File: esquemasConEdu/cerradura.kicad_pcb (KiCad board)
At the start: 2 copper layers, 85.8 x 137 mm, 16 parts, among them Q1 PN2222A

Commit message: conectado
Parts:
- moved A3144 119.0 mm to (72.1, 176.9), turned to 180 degrees
- moved 10K1 117.8 mm to (61.0, 154.9), turned to -90 degrees
- moved MOTOR_BORN1 96.7 mm to (122.8, 176.7), turned to 180 degrees
- moved Q1 95.6 mm to (63.1, 150.7)
- moved BUZZER1 80.0 mm to (67.8, 139.7), turned to 180 degrees
- moved 5V_BORN1 76.8 mm to (123.2, 58.4), turned to -90 degrees
- moved RC522 50.3 mm to (93.4, 127.9), turned to 90 degrees
- moved lm2596hvs1 47.4 mm to (90.9, 60.3), turned to 0 degrees
- moved R305 38.9 mm to (58.4, 89.2)
- moved 12V-BORN1 30.9 mm to (54.5, 51.8), turned to 90 degrees
- moved SSD1306 26.0 mm to (107.9, 89.3), turned to 90 degrees
- moved DRV8825 25.7 mm to (95.5, 178.5)
- moved Keypad1 18.8 mm to (109.2, 160.7), turned to 180 degrees
- moved ESP1 10.5 mm to (113.6, 134.3)
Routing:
- net GND: track 0.00 -> 480.5 mm
- net +5V: track 0.00 -> 226.1 mm
- net +12V: track 0.00 -> 207.4 mm
- net +3.3V: track 0.00 -> 205.6 mm
- net /drv882x_en: track 0.00 -> 87.8 mm
- net /r305_rx: track 0.00 -> 78.4 mm
- net /ssd1306_scl: track 0.00 -> 77.1 mm
- net /r305_tx: track 0.00 -> 74.8 mm
- net /rc522-ss: track 0.00 -> 69.9 mm
- net /ssd1306_sda: track 0.00 -> 68.3 mm
- net /drv882x_step: track 0.00 -> 64.7 mm
- net /rc522-mosi: track 0.00 -> 50.8 mm
- net /rc522-rst: track 0.00 -> 49.0 mm
- net /rc522-sck: track 0.00 -> 48.3 mm
- net /rc522-irq: track 0.00 -> 46.1 mm
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
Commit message: jack por bornera
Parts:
- 12V-BORN1: value Jack-DC -> 12V-DC-IN; footprint Connector_BarrelJack:BarrelJack_SwitchcraftConxall_RAPC10U_Horizontal -> TerminalBlock:TerminalBlock_Altech_AK300-2_P5.00mm
- moved 12V-BORN1 5.25 mm to (53.1, 56.8)
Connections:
- 12V-BORN1 pad 1: +12V -> GND
- 12V-BORN1 pad 2: GND -> +12V

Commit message: eliminacion pines sobrados
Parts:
- moved BUZZER1 27.8 mm to (75.8, 113.2)
- moved 10K1 14.4 mm to (54.5, 167.7)
- moved A3144 8.50 mm to (63.6, 176.7)
- moved Q1 8.49 mm to (71.5, 152.2)
- moved 12V-BORN1 5.53 mm to (56.4, 61.3)
- moved MOTOR_BORN1 2.68 mm to (120.2, 176.6)
- moved DRV8825 2.47 mm to (93.0, 178.3)
- moved lm2596hvs1 0.37 mm to (90.9, 60.7)
- moved 5V_BORN1 0.30 mm to (122.9, 58.3)
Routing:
- net GND: track 480.5 -> 0.00 mm
- net +5V: track 226.1 -> 0.00 mm
- net +12V: track 207.4 -> 0.00 mm
- net +3.3V: track 205.6 -> 0.00 mm
- net /drv882x_en: track 87.8 -> 0.00 mm
- net /r305_rx: track 78.4 -> 0.00 mm
- net /ssd1306_scl: track 77.1 -> 0.00 mm
- net /r305_tx: track 74.8 -> 0.00 mm
- net /rc522-ss: track 69.9 -> 0.00 mm
- net /ssd1306_sda: track 68.3 -> 0.00 mm
- net /drv882x_step: track 64.7 -> 0.00 mm
- net /rc522-mosi: track 50.8 -> 0.00 mm
- net /rc522-rst: track 49.0 -> 0.00 mm
- net /rc522-sck: track 48.3 -> 0.00 mm
- net /rc522-irq: track 46.1 -> 0.00 mm
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
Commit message: plano de tierra
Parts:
- moved Keypad1 3.82 mm to (107.3, 163.9)
- moved Q1 1.99 mm to (73.1, 153.3)
- moved DRV8825 0.32 mm to (93.2, 178.6)
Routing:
- added copper zone on B.Cu, net GND
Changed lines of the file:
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@@
 	(generator_version "9.0")
 	(general
-		(thickness 1.6)
+		(thickness 1.59)
 		(legacy_teardrops no)
 	)
@@
 		(0 "F.Cu" signal)
 		(2 "B.Cu" signal)
-		(9 "F.Adhes" user "F.Adhesive")
-		(11 "B.Adhes" user "B.Adhesive")
-		(13 "F.Paste" user)
-		(15 "B.Paste" user)
 		(5 "F.SilkS" user "F.Silkscreen")
-		(7 "B.SilkS" user "B.Silkscreen")
-		(1 "F.Mask" user)
 		(3 "B.Mask" user)
-		(17 "Dwgs.User" user "User.Drawings")
-		(19 "Cmts.User" user "User.Comments")
-		(21 "Eco1.User" user "User.Eco1")
-		(23 "Eco2.User" user "User.Eco2")
 		(25 "Edge.Cuts" user)
 		(27 "Margin" user)
 		(31 "F.CrtYd" user "F.Courtyard")
 		(29 "B.CrtYd" user "B.Courtyard")
-		(35 "F.Fab" user)
-		(33 "B.Fab" user)
-		(39 "User.1" user)
-		(41 "User.2" user)
-		(43 "User.3" user)
-		(45 "User.4" user)
 	)
 	(setup
+		(stackup
+			(layer "F.SilkS"
+				(type "Top Silk Screen")
+			)
+			(layer "F.Cu"
+				(type "copper")
+				(thickness 0.035)
+			)
+			(layer "dielectric 1"
+				(type "core")
+				(thickness 1.51)
+				(material "FR4")
+				(epsilon_r 4.5)
+				(loss_tangent 0.02)
+			)
+			(layer "B.Cu"
+				(type "copper")
+				(thickness 0.035)
+			)
+			(layer "B.Mask"
+				(type "Bottom Solder Mask")
+				(thickness 0.01)
+			)
+			(copper_finish "None")
+			(dielectric_constraints no)
+		)
 		(pad_to_mask_clearance 0)
 		(allow_soldermask_bridges_in_footprints no)
@@
 	(footprint "Connector_PinSocket_2.54mm:PinSocket_1x08_P2.54mm_Vertical"
 		(layer "F.Cu")
-		(at 109.24 160.66 180)
+		(at 107.26 163.93 180)
 		(descr "Through hole straight socket strip, 1x08, 2.54mm pitch, single row (from Kicad 4.0.7), script generated")
 		(tags "Through hole socket strip THT 1x08 2.54mm single row")
@@
 	(footprint "Package_TO_SOT_THT:TO-92_Inline"
 		(layer "F.Cu")
-		(at 71.51 152.16 180)
+		(at 73.13 153.31 180)
 		(descr "TO-92 leads in-line, narrow, oval pads, drill 0.75mm (see NXP sot054_po.pdf)")
 		(tags "to-92 sc-43 sc-43a sot54 PA33 transistor")
@@
 	(footprint "Module:Pololu_Breakout-16_15.2x20.3mm"
 		(layer "F.Cu")
-		(at 92.99 178.3 180)
+		(at 93.17 178.57 180)
 		(descr "Pololu Breakout 16-pin 15.2x20.3mm 0.6x0.8")
 		(tags "Pololu Breakout")
@@
 		(layer "Edge.Cuts")
 	)
+	(zone
+		(net 5)
+		(net_name "GND")
+		(layer "B.Cu")
+		(hatch edge 0.5)
+		(connect_pads
+			(clearance 0.5)
+		)
+		(min_thickness 0.25)
+		(filled_areas_thickness no)
+		(fill yes
+			(thermal_gap 0.5)
+			(thermal_bridge_width 0.5)
+		)
+		(polygon
+			(pts
+				(xy 50.73 185.03) (xy 128.42 184.93) (xy 130.29 183.99) (xy 131.03 182.42) (xy 131.13 50.76) (xy 130.29 49.51)
+				(xy 128.42 48.57) (xy 48.64 48.57) (xy 46.45 49.3) (xy 45.62 50.86) (xy 45.72 182.42) (xy 46.45 183.99)
+				(xy 48.12 184.93) (xy 51.46 184.93) (xy 51.05 185.14)
+			)
+		)
+	)
 	(embedded_fonts no)

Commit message: acomode
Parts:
- moved A3144 107.8 mm to (52.6, 69.5), turned to -90 degrees
- moved 10K1 81.4 mm to (53.6, 86.3)
- moved R305 79.5 mm to (77.2, 166.4)
- moved Q1 52.4 mm to (65.6, 101.5), turned to 90 degrees
- moved DRV8825 43.3 mm to (50.0, 181.7), turned to 90 degrees
- moved RC522 39.7 mm to (113.0, 162.4)
- moved ESP1 32.7 mm to (95.1, 107.4)
- moved Keypad1 29.2 mm to (100.4, 135.6)
- moved BUZZER1 28.7 mm to (54.5, 93.9), turned to -90 degrees
- moved MOTOR_BORN1 27.8 mm to (92.3, 176.7)
- moved SSD1306 8.57 mm to (116.0, 86.6)
- moved 5V_BORN1 4.39 mm to (119.7, 55.4)
- moved 12V-BORN1 2.65 mm to (58.8, 60.1)
- moved lm2596hvs1 1.82 mm to (89.8, 59.2)

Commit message: update
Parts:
- moved Keypad1 43.8 mm to (111.9, 177.8)
- moved RC522 40.5 mm to (84.7, 133.3)
- moved DRV8825 28.0 mm to (77.9, 179.9)
- moved R305 27.9 mm to (63.1, 142.3), turned to 0 degrees
- moved MOTOR_BORN1 24.9 mm to (67.5, 175.3)
- moved ESP1 5.01 mm to (90.1, 107.1)
- moved SSD1306 2.04 mm to (114.1, 85.8)
- moved A3144 1.03 mm to (53.6, 69.5)
- moved BUZZER1 0.74 mm to (54.0, 93.4)
- moved Q1 0.40 mm to (66.0, 101.4)
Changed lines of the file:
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@@
 	(footprint "TerminalBlock:TerminalBlock_Altech_AK300-2_P5.00mm"
 		(layer "F.Cu")
-		(at 54.54 93.885 -90)
+		(at 54 93.385 -90)
 		(descr "Altech AK300 terminal block, pitch 5.0mm, 45 degree angled, see http://www.mouser.com/ds/2/16/PCBMETRC-24178.pdf")
 		(tags "Altech AK300 terminal block pitch 5.0mm")
 		(property "Reference" "BUZZER1"
-			(at -1.92 -6.99 90)
+			(at 1.255 -5.13 90)
 			(layer "F.SilkS")
 			(effects
@@
 	(footprint "Connector_PinSocket_2.54mm:PinSocket_1x04_P2.54mm_Vertical"
 		(layer "F.Cu")
-		(at 77.18 166.4 90)
+		(at 63.1 142.27)
 		(descr "Through hole straight socket strip, 1x04, 2.54mm pitch, single row (from Kicad 4.0.7), script generated")
 		(tags "Through hole socket strip THT 1x04 2.54mm single row")
 		(property "Reference" "R305"
-			(at 2.715 3.2 0)
+			(at 2.715 3.2 90)
 			(layer "F.SilkS")
 			(effects
@@
 		)
 		(property "Value" "R305_sensor"
-			(at -2.985 4.22 0)
+			(at -2.985 4.22 90)
 			(layer "F.Fab")
 			(hide yes)
@@
 		)
 		(property "Datasheet" "~"
-			(at 0 0 90)
+			(at 0 0 0)
 			(layer "F.Fab")
 			(hide yes)
@@
 		)
 		(property "Description" "Generic connector, single row, 01x04, script generated"
-			(at 0 0 90)
+			(at 0 0 0)
 			(layer "F.Fab")
 			(hide yes)
@@
 		(attr through_hole)
 		(fp_line
-			(start 1.33 -1.33)
-			(end 1.33 0)
+			(start -1.33 1.27)
+			(end -1.33 8.95)
 			(stroke
 				(width 0.12)
@@
 		)
 		(fp_line
-			(start 0 -1.33)
-			(end 1.33 -1.33)
+			(start -1.33 1.27)
+			(end 1.33 1.27)
 			(stroke
 				(width 0.12)
@@
 		)
 		(fp_line
-			(start 1.33 1.27)
+			(start -1.33 8.95)
 			(end 1.33 8.95)
 			(stroke
@@
 		)
 		(fp_line
-			(start -1.33 1.27)
-			(end 1.33 1.27)
+			(start 0 -1.33)
+			(end 1.33 -1.33)
 			(stroke
 				(width 0.12)
@@
 		)
 		(fp_line
-			(start -1.33 1.27)
-			(end -1.33 8.95)
+			(start 1.33 -1.33)
+			(end 1.33 0)
 			(stroke
 				(width 0.12)
@@
 		)
 		(fp_line
-			(start -1.33 8.95)
+			(start 1.33 1.27)
 			(end 1.33 8.95)
 			(stroke
@@
 		)
 		(fp_line
-			(start 1.75 -1.8)
-			(end 1.75 9.4)
+			(start -1.8 -1.8)
+			(end 1.75 -1.8)
 			(stroke
 				(width 0.05)
@@
 		)
 		(fp_line
-			(start -1.8 -1.8)
-			(end 1.75 -1.8)
+			(start -1.8 9.4)
+			(end -1.8 -1.8)
 			(stroke
 				(width 0.05)
@@
 		)
 		(fp_line
-			(start 1.75 9.4)
-			(end -1.8 9.4)
+			(start 1.75 -1.8)
+			(end 1.75 9.4)
 			(stroke
 				(width 0.05)
@@
 		)
 		(fp_line
-			(start -1.8 9.4)
-			(end -1.8 -1.8)
+			(start 1.75 9.4)
+			(end -1.8 9.4)
 			(stroke
 				(width 0.05)
@@
 		)
 		(fp_line
-			(start 0.635 -1.27)
-			(end 1.27 -0.635)
+			(start -1.27 -1.27)
+			(end 0.635 -1.27)
 			(stroke
 				(width 0.1)
@@
 		)
 		(fp_line
-			(start -1.27 -1.27)
-			(end 0.635 -1.27)
+			(start -1.27 8.89)
+			(end -1.27 -1.27)
 			(stroke
 				(width 0.1)
@@
 		)
 		(fp_line
-			(start 1.27 -0.635)
-			(end 1.27 8.89)
+			(start 0.635 -1.27)
+			(end 1.27 -0.635)
 			(stroke
 				(width 0.1)
@@
 		)
 		(fp_line
-			(start 1.27 8.89)
-			(end -1.27 8.89)
+			(start 1.27 -0.635)
+			(end 1.27 8.89)
 			(stroke
 				(width 0.1)
@@
 		)
 		(fp_line
-			(start -1.27 8.89)
-			(end -1.27 -1.27)
+			(start 1.27 8.89)
+			(end -1.27 8.89)
 			(stroke
 				(width 0.1)
@@
 		)
 		(fp_text user "${REFERENCE}"
-			(at -0.025 3.8 0)
+			(at -0.025 3.8 90)
 			(layer "F.Fab")
 			(effects
@@
 		)
 		(pad "1" thru_hole rect
-			(at 0 0 90)
+			(at 0 0)
 			(size 1.7 1.7)
 			(drill 1)
@@
 		)
 		(pad "2" thru_hole circle
-			(at 0 2.54 90)
+			(at 0 2.54)
 			(size 1.7 1.7)
 			(drill 1)
@@
 		)
 		(pad "3" thru_hole circle
-			(at 0 5.08 90)
+			(at 0 5.08)
 			(size 1.7 1.7)
 			(drill 1)
@@
 		)
 		(pad "4" thru_hole circle
-			(at 0 7.62 90)
+			(at 0 7.62)
 			(size 1.7 1.7)
 			(drill 1)
@@
 	(footprint "TerminalBlock:TerminalBlock_Altech_AK300-4_P5.00mm"
 		(layer "F.Cu")
-		(at 92.35 176.69 180)
+		(at 67.47 175.33 180)
 		(descr "Altech AK300 terminal block, pitch 5.0mm, 45 degree angled, see http://www.mouser.com/ds/2/16/PCBMETRC-24178.pdf")
 		(tags "Altech AK300 terminal block pitch 5.0mm")
@@
 	(footprint "Connector_PinSocket_2.54mm:PinSocket_1x08_P2.54mm_Vertical"
 		(layer "F.Cu")
-		(at 100.37 135.55 180)
+		(at 111.91 177.82 180)
 		(descr "Through hole straight socket strip, 1x08, 2.54mm pitch, single row (from Kicad 4.0.7), script generated")
 		(tags "Through hole socket strip THT 1x08 2.54mm single row")
@@
 	(footprint "Package_TO_SOT_THT:TO-92_Inline"
 		(layer "F.Cu")
-		(at 65.62 101.46 90)
+		(at 66.01 101.39 90)
 		(descr "TO-92 leads in-line, narrow, oval pads, drill 0.75mm (see NXP sot054_po.pdf)")
 		(tags "to-92 sc-43 sc-43a sot54 PA33 transistor")
@@
 	(footprint "Connector_PinSocket_2.54mm:PinSocket_1x04_P2.54mm_Vertical"
 		(layer "F.Cu")
-		(at 116 86.63 90)
+		(at 114.12 85.85 90)
 		(descr "Through hole straight socket strip, 1x04, 2.54mm pitch, single row (from Kicad 4.0.7), script generated")
 		(tags "Through hole socket strip THT 1x04 2.54mm single row")
@@
 	(footprint "Module:Pololu_Breakout-16_15.2x20.3mm"
 		(layer "F.Cu")
-		(at 49.99 181.73 90)
+		(at 77.92 179.88 90)
 		(descr "Pololu Breakout 16-pin 15.2x20.3mm 0.6x0.8")
 		(tags "Pololu Breakout")
@@
 	(footprint "TerminalBlock:TerminalBlock_Altech_AK300-3_P5.00mm"
 		(layer "F.Cu")
-		(at 52.62 69.51 -90)
+		(at 53.65 69.47 -90)
 		(descr "Altech AK300 terminal block, pitch 5.0mm, 45 degree angled, see http://www.mouser.com/ds/2/16/PCBMETRC-24178.pdf")
 		(tags "Altech AK300 terminal block pitch 5.0mm")
 		(property "Reference" "A3144"
-			(at 5.48 -7.45 90)
+			(at 1.02 -7.81 90)
 			(layer "F.SilkS")
 			(effects
@@
 	(footprint "Connector_PinSocket_2.54mm:PinSocket_2x08_P2.54mm_Vertical"
 		(layer "F.Cu")
-		(at 95.08 107.425 180)
+		(at 90.08 107.105 180)
 		(descr "Through hole straight socket strip, 2x08, 2.54mm pitch, double cols (from Kicad 4.0.7), script generated")
 		(tags "Through hole socket strip THT 2x08 2.54mm double row")
 		(property "Reference" "ESP1"
-			(at 5.2 2.52 0)
+			(at 6.86 2.795 0)
 			(layer "F.SilkS")
 			(effects
@@
 			(layer "F.SilkS")
 			(pts
-				(xy 97.62 107.425) (xy 82.38 107.425)
+				(xy 92.62 107.105) (xy 77.38 107.105)
 			)
 			(height -8.9)
@@
 				(keep_text_aligned yes)
 			)
-			(gr_text "15,24"
-				(at 90 97.425 0)
+			(gr_text "600"
+				(at 85 97.105 0)
 				(layer "F.SilkS")
 				(effects
@@
 			(layer "F.SilkS")
 			(pts
-				(xy 98.95 88.315) (xy 80.95 87.865)
+				(xy 93.95 87.995) (xy 75.95 87.545)
 			)
 			(height 5.21)
@@
 				(keep_text_aligned yes)
 			)
-			(gr_text "18"
-				(at 89.95 92.425 0)
+			(gr_text "708,6614"
+				(at 84.95 92.105 0)
 				(layer "F.SilkS")
 				(effects
@@
 	(footprint "Connector_PinSocket_2.54mm:PinSocket_1x08_P2.54mm_Vertical"
 		(layer "F.Cu")
-		(at 113.03 162.36 90)
+		(at 84.72 133.33 90)
 		(descr "Through hole straight socket strip, 1x08, 2.54mm pitch, single row (from Kicad 4.0.7), script generated")
 		(tags "Through hole socket strip THT 1x08 2.54mm single row")
@@
 			)
 		)
-		(dimension
-			(type orthogonal)
-			(layer "F.SilkS")
-			(pts
-				(xy 99.51 180.1) (xy 100.65 141.09)
-			)
-			(height 55.64)
-			(orientation 1)
-			(format
-				(prefix "")
-				(suffix "")
-				(units 3)
-				(units_format 0)
-				(precision 4)
-				(suppress_zeroes yes)
-			)
-			(style
-				(thickness 0.1)
-				(arrow_length 1.27)
-				(text_position_mode 0)
-				(arrow_direction outward)
-				(extension_height 0.58642)
-				(extension_offset 0.5)
-				(keep_text_aligned yes)
-			)
-			(gr_text "39,01"
-				(at 154.05 160.595 90)
-				(layer "F.SilkS")
-				(effects
-					(font
-						(size 1 1)
-						(thickness 0.1)
-					)
-				)
-			)
-		)
-		(dimension
-			(type orthogonal)
-			(layer "F.SilkS")
-			(pts
-				(xy 99.51 176.97) (xy 158.51 174.04)
-			)
-			(height 0.33)
-			(orientation 0)
-			(format
-				(prefix "")
-				(suffix "")
-				(units 3)
-				(units_format 0)
-				(precision 4)
-				(suppress_zeroes yes)
-			)
-			(style
-				(thickness 0.1)
-				(arrow_length 1.27)
-				(text_position_mode 0)
-				(arrow_direction outward)
-				(extension_height 0.58642)
-				(extension_offset 0.5)
-				(keep_text_aligned yes)
-			)
-			(gr_text "59"
-				(at 129.01 176.2 0)
-				(layer "F.SilkS")
-				(effects
-					(font
-						(size 1 1)
-						(thickness 0.1)
-					)
-				)
-			)
-		)

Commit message: .
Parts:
- moved DRV8825 28.1 mm to (49.9, 181.2)
- moved R305 25.0 mm to (77.0, 163.0), turned to 180 degrees
- moved MOTOR_BORN1 22.6 mm to (90.0, 173.5)
- moved 10K1 8.93 mm to (62.5, 86.0), turned to 180 degrees
- moved RC522 4.48 mm to (83.0, 129.2), turned to -90 degrees

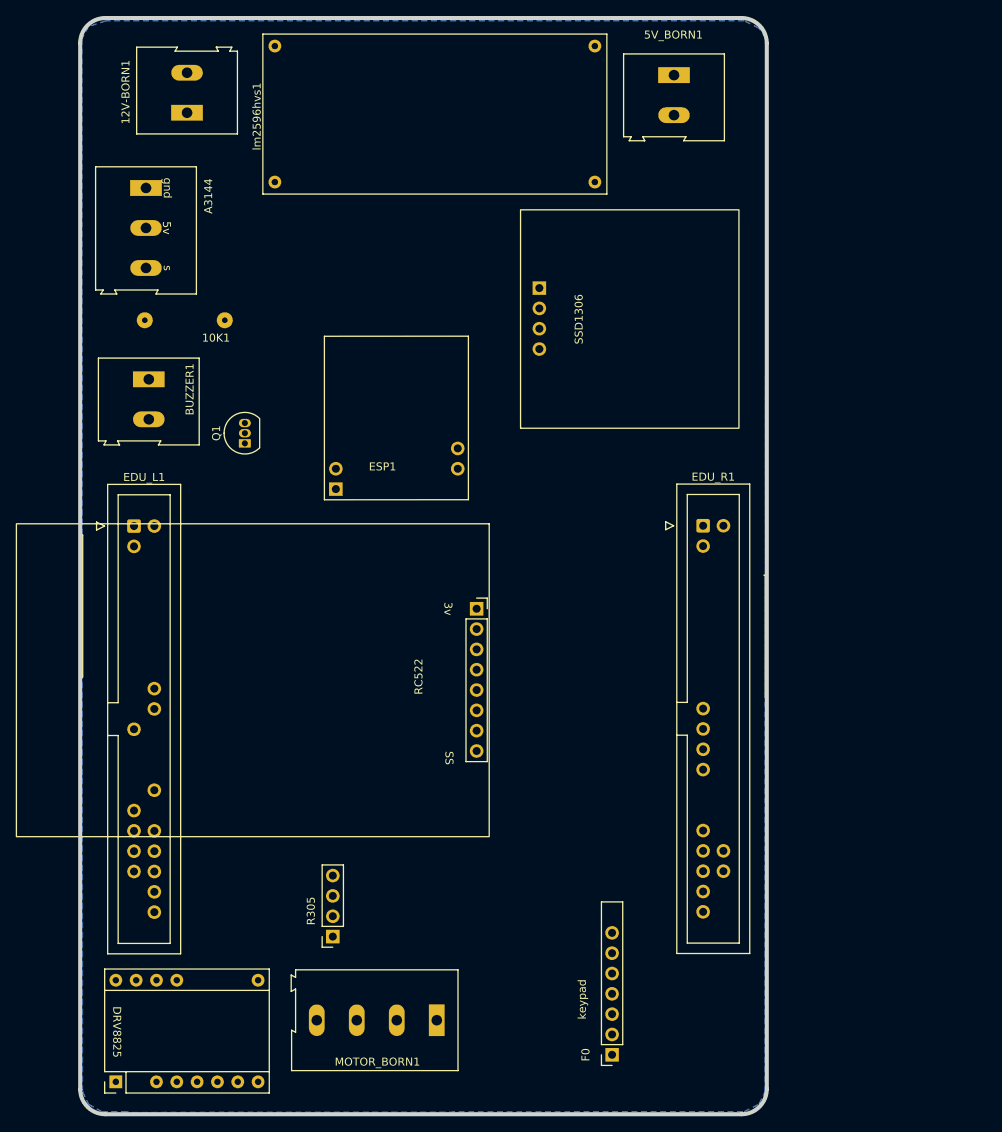
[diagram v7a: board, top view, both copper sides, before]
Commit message: todo conectado + algunas vias
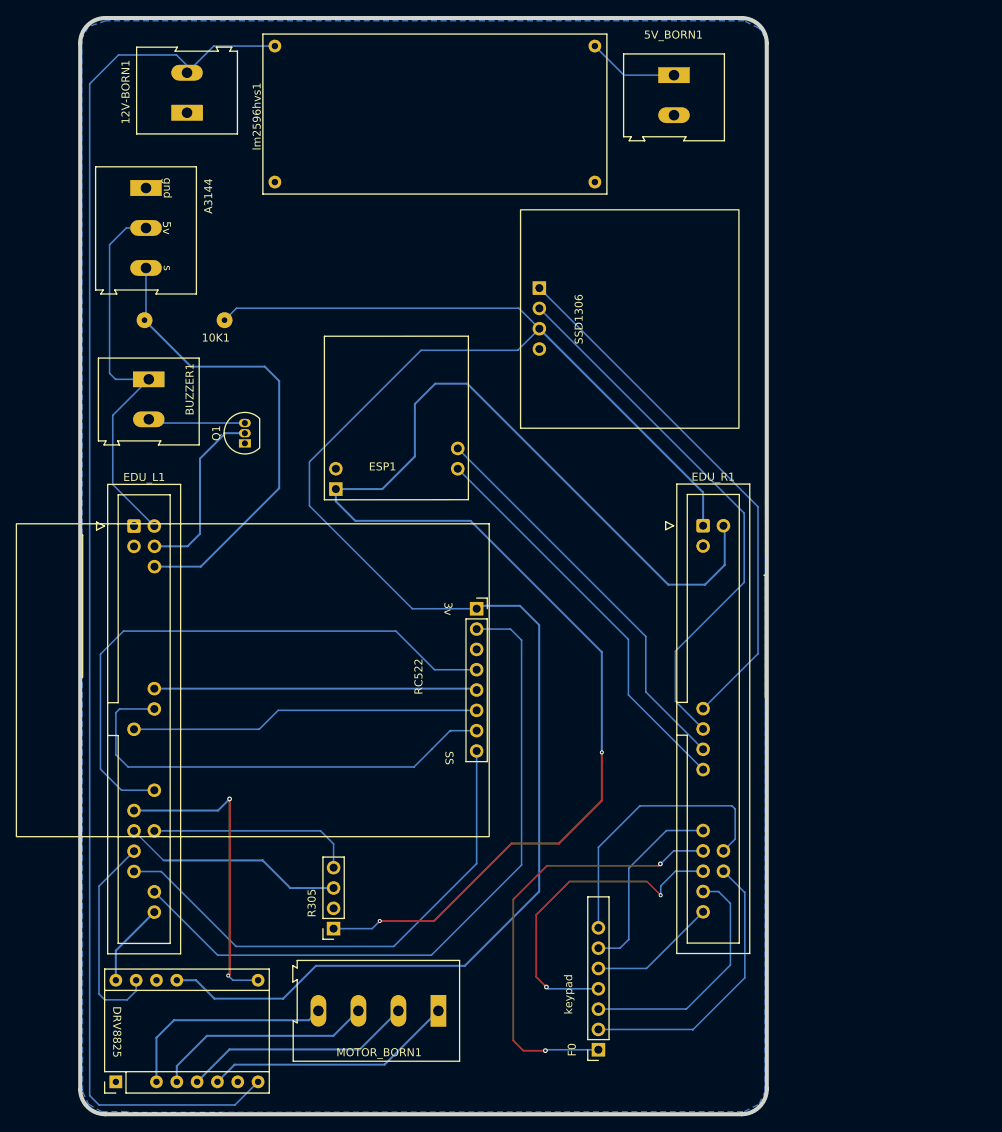
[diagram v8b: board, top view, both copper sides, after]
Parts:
- moved Keypad1 1.82 mm to (110.2, 177.2)
- moved MOTOR_BORN1 1.19 mm to (90.2, 172.3)
- moved R305 1.00 mm to (77.1, 162.1)
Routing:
- net +3.3V: track 0.00 -> 235.6 mm
- net +5V: track 0.00 -> 224.7 mm, vias 0 -> 2
- net +12V: track 0.00 -> 176.7 mm
- net /rc522-rst: track 0.00 -> 88.2 mm
- net /rc522-irq: track 0.00 -> 72.4 mm
- net /ssd1306_scl: track 0.00 -> 68.2 mm
- net /ssd1306_sda: track 0.00 -> 66.7 mm
- net /rc522-ss: track 0.00 -> 65.1 mm
- net /door_sensor: track 0.00 -> 59.6 mm
- net /rc522-sck: track 0.00 -> 57.9 mm
- net /kp_f0: track 0.00 -> 55.1 mm, vias 0 -> 2
- net /esp32_tx: track 0.00 -> 50.3 mm
- net /esp32_rx: track 0.00 -> 50.3 mm
- net /rc522-mosi: track 0.00 -> 43.8 mm
- net /kp_f3: track 0.00 -> 41.4 mm, vias 0 -> 2
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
